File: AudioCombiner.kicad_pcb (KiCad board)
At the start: 2 copper layers, 27.9 x 33 mm, 8 parts, among them J1 Primary, J2 Secondary, J3 Headphones

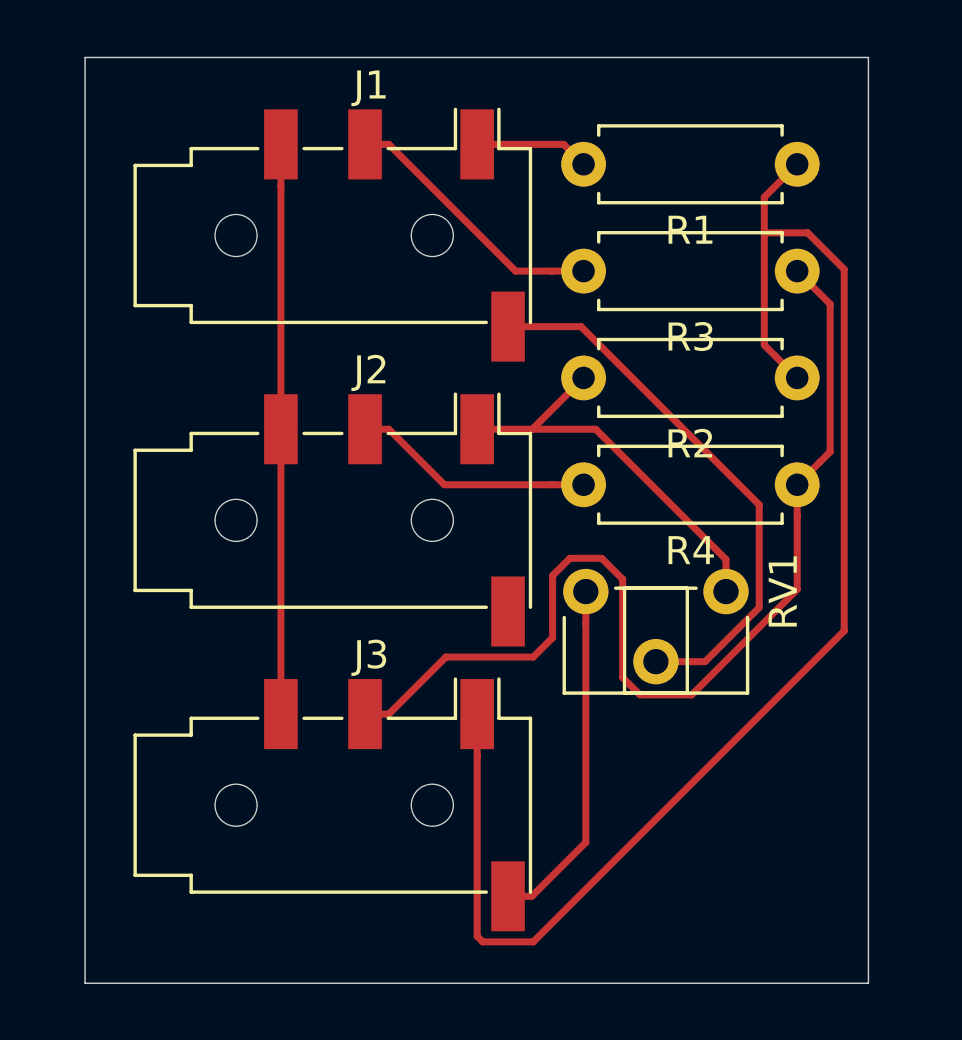
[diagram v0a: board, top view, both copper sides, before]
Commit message: THT audio jack
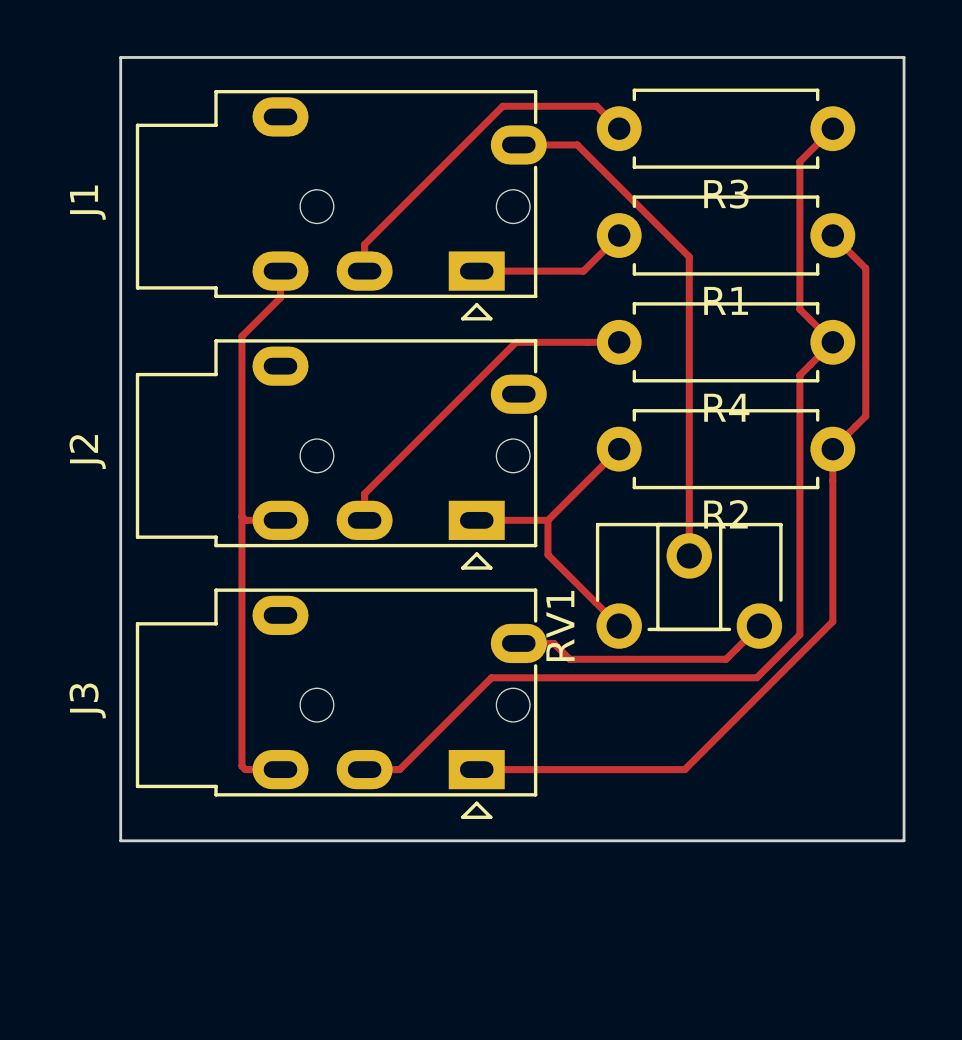
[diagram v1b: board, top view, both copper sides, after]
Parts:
- J1, J2, J3: footprint Connector_Audio:Jack_3.5mm_PJ320D_Horizontal -> Connector_Audio:Jack_3.5mm_PJ320E_Horizontal
- moved R4 5.24 mm to (39.4, 22.9)
- moved R3 5.24 mm to (39.4, 15.2)
- moved J1 4.02 mm to (26.7, 20.3), turned to 90 degrees
- moved J3 4.02 mm to (26.7, 38.1), turned to 90 degrees
- moved RV1 4.00 mm to (31.8, 33.0), turned to 90 degrees
- moved J2 3.81 mm to (26.7, 29.2), turned to 90 degrees
- moved R2 2.84 mm to (39.4, 26.7)
- moved R1 2.84 mm to (39.4, 19.1)
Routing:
- net Net-(J3-PadT): track 50.6 -> 29.6 mm
- net Net-(J2-PadR1): track 8.62 -> 12.3 mm
- net Net-(J2-PadT): track 14.5 -> 11.0 mm
- net Net-(J3-PadS): track 12.5 -> 9.30 mm
- net Net-(J1-PadR1): track 9.67 -> 12.4 mm
- net Net-(J1-PadT): track 4.09 -> 5.61 mm
- net Net-(J1-PadS): track 19.7 -> 18.4 mm
- net Net-(J1-PadR2): track 20.3 -> 21.1 mm
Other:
- board size 27.9 x 33 mm -> 27.9 x 27.9 mm
